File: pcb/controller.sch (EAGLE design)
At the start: 5 parts, among them IC1 74LS595D, IC2 74LS595D, IC3 FT232RL, U1 ATMEGA328P-PU, X1 MINI-USB_SHIELD5P4-32005-400

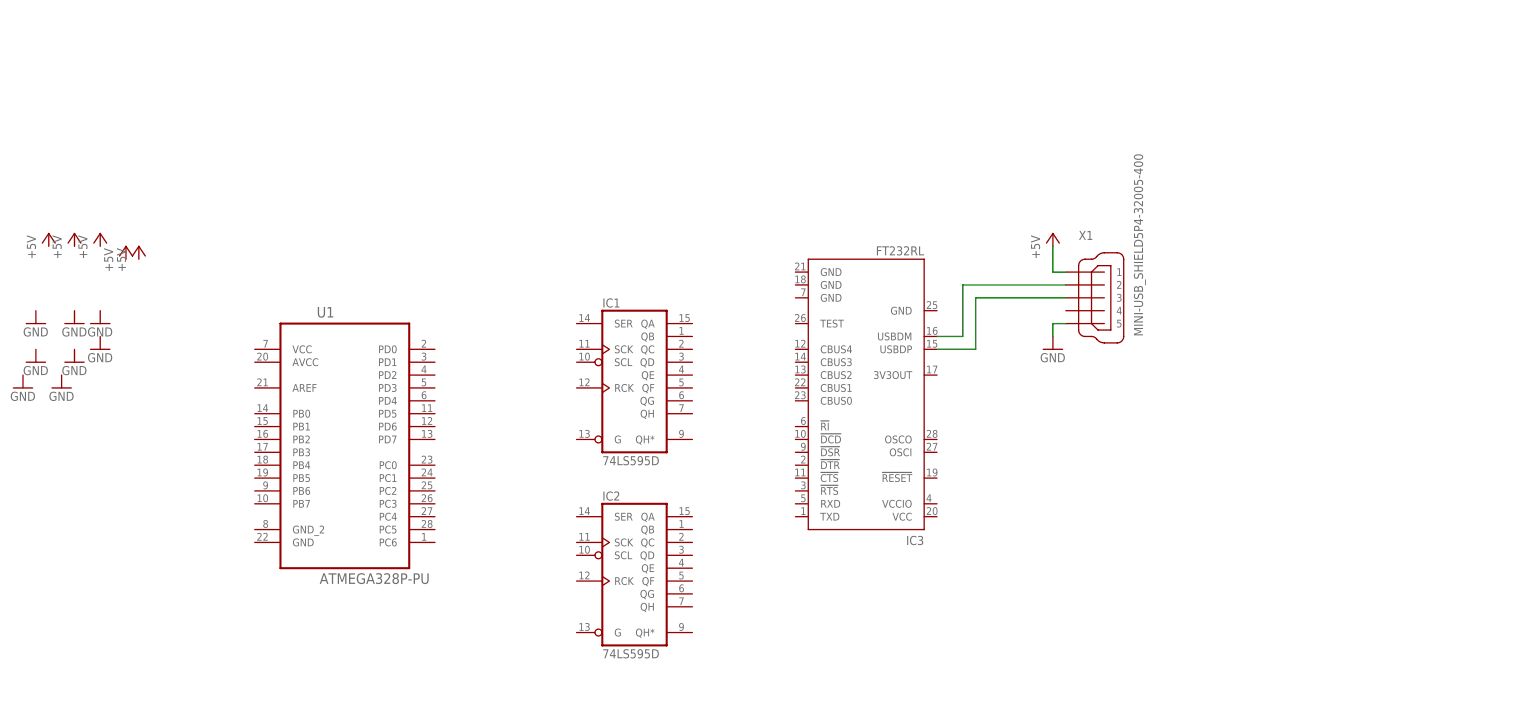
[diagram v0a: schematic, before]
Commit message: Connected FTDI and atmega328
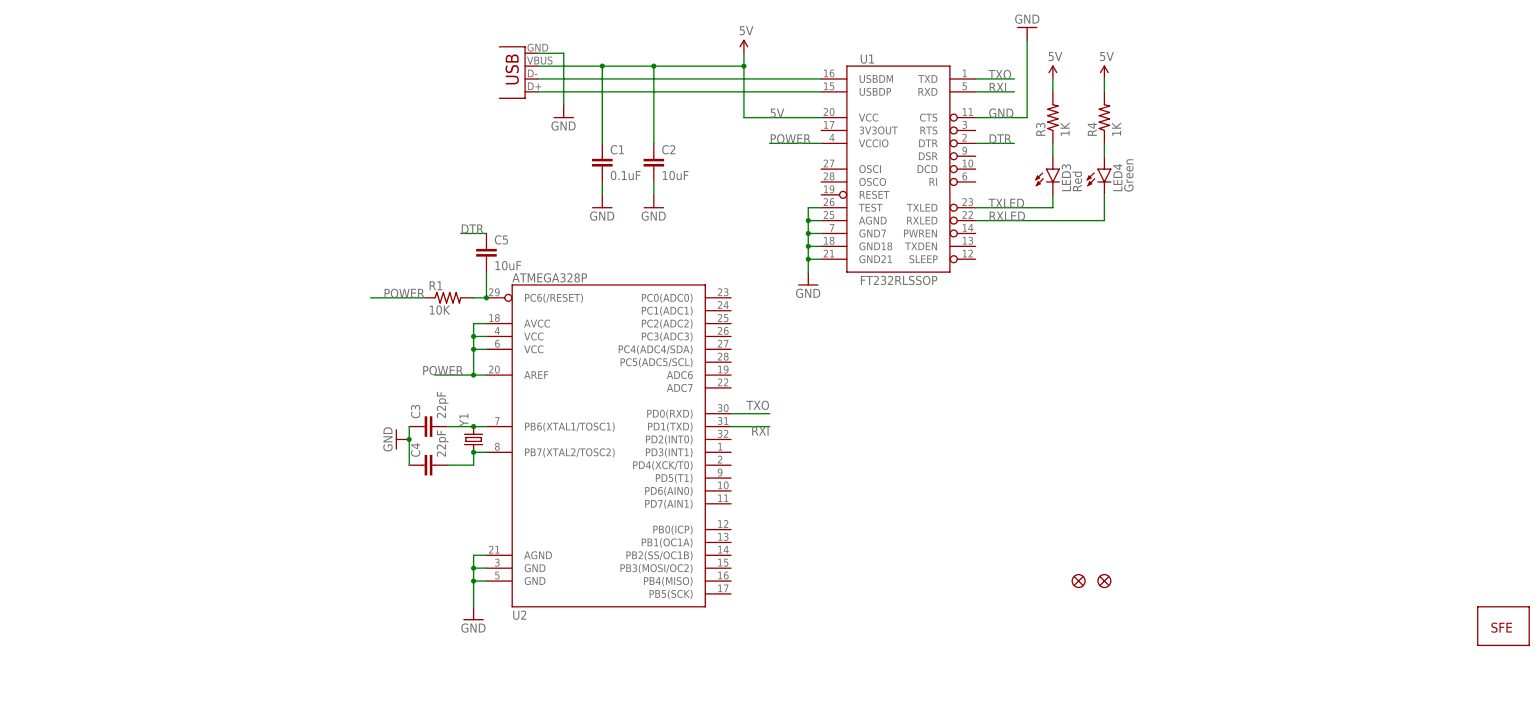
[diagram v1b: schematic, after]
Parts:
- removed IC1, IC2: 74LS595D, 74xx-us:74LS595D
- removed IC3: FT232RL, ftdichip:FT232RL
- removed X1: MINI-USB_SHIELD5P4-32005-400, con-cypressindustries:MINI-USB_SHIELD5P4-32005-400
- added C1: 0.1uF, SparkFun-Capacitors:CAP0805
- added C2, C5: 10uF, SparkFun-Capacitors:CAP0805
- added C3, C4: 22pF, SparkFun-Capacitors:CAP0805
- added JP8, JP9: FIDUCIAL1X2, SparkFun:FIDUCIAL1X2
- added LED3: Red, SparkFun-LED:LED1206
- added LED4: Green, SparkFun-LED:LED1206
- added R1: 10K, SparkFun-Resistors:RESISTOR0805-RES
- added R3, R4: 1K, SparkFun-Resistors:RESISTOR0805-RES
- added U$2: LOGO-SFENW2, SparkFun:LOGO-SFENW2
- added U2: ATMEGA328P, SparkFun-DigitalIC:ATMEGA328_SMT
- added X2: USB-SMD-NS, SparkFun:USB-SMD-NS
- added Y1: (no value), SparkFun-FreqCtrl:CRYSTALHC49US
- U1: value ATMEGA328P-PU -> FT232RLSSOP; device Atmel_By_element14_Batch_1-00:ATMEGA328P-PU -> SparkFun:FT232RLSSOP
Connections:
- removed net +5V: X1G$1.1
- new net 5V: C1.1, C2.1, R3.2, R4.2, U1.VCC, X2.VBUS
- new net DTR: C5.1, U1.DTR
- new net N$3: C5.2, R1.2, U2.PC6(/RESET)
- new net N$7: C3.2, U2.PB6(XTAL1/TOSC1), Y1.2
- new net N$8: C4.2, U2.PB7(XTAL2/TOSC2), Y1.1
- new net POWER: R1.1, U1.VCCIO, U2.AREF, U2.AVCC, U2.VCC@1, U2.VCC@2
- new net RXI: U1.RXD, U2.PD1(TXD)
- new net RXLED: LED4.C, U1.RXLED
- new net TXLED: LED3.C, U1.TXLED
- new net TXO: U1.TXD, U2.PD0(RXD)
- new net USB_D+: U1.USBDP, X2.D+
- new net USB_D-: U1.USBDM, X2.D-
- net GND: now also C1.2, C2.2, C3.1, C4.1, U1.AGND, U1.CTS, U1.GND18, U1.GND21, U1.GND7, U1.TEST, U2.AGND, U2.GND@1, U2.GND@2, X2.GND; no longer X1G$1.5
- net N$1: now also LED3.A, R3.1; no longer IC3.USBDM, X1G$1.2
- net N$2: now also LED4.A, R4.1; no longer IC3.USBDP, X1G$1.3

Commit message: Added ISCP to atmega328
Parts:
- added ICSP: (no value), SparkFun-Connectors:M03X2POGO_PINS
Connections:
- removed net N$3: C5.2, R1.2, U2.PC6(/RESET)
- new net MISO: ICSP.1, U2.PB4(MISO)
- new net MOSI: ICSP.4, U2.PB3(MOSI/OC2)
- new net RESET: C5.2, ICSP.5, R1.2, U2.PC6(/RESET)
- new net SCK: ICSP.3, U2.PB5(SCK)
- net GND: now also ICSP.6
- net POWER: now also ICSP.2
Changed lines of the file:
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@@
 <part name="C5" library="SparkFun-Capacitors" deviceset="CAP" device="0805" value="10uF"/>
 <part name="GND4" library="SparkFun" deviceset="GND" device=""/>
+<part name="ICSP" library="SparkFun-Connectors" deviceset="M03X2" device="POGO_PINS"/>
 </parts>
 <sheets>
@@
 <instance part="C5" gate="G$1" x="43.18" y="91.44"/>
 <instance part="GND4" gate="1" x="149.86" y="137.16" rot="R180"/>
+<instance part="ICSP" gate="G$1" x="68.58" y="10.16"/>
 </instances>
 <busses>
@@
 <pinref part="GND4" gate="1" pin="GND"/>
 </segment>
+<segment>
+<pinref part="ICSP" gate="G$1" pin="6"/>
+<wire x1="76.2" y1="7.62" x2="83.82" y2="7.62" width="0.1524" layer="91"/>
+<label x="76.2" y="7.62" size="1.778" layer="95"/>
+</segment>
 </net>
 <net name="USB_D-" class="0">
@@
 <wire x1="30.48" y1="83.82" x2="20.32" y2="83.82" width="0.1524" layer="91"/>
 <label x="22.86" y="83.82" size="1.778" layer="95"/>
+</segment>
+<segment>
+<pinref part="ICSP" gate="G$1" pin="2"/>
+<wire x1="76.2" y1="12.7" x2="83.82" y2="12.7" width="0.1524" layer="91"/>
+<label x="76.2" y="12.7" size="1.778" layer="95"/>
 </segment>
 </net>
@@
 </segment>
 </net>
-<net name="N$3" class="0">
-<segment>
-<pinref part="U2" gate="G$1" pin="PC6(/RESET)"/>
-<wire x1="43.18" y1="83.82" x2="40.64" y2="83.82" width="0.1524" layer="91"/>
-<pinref part="R1" gate="G$1" pin="2"/>
-<pinref part="C5" gate="G$1" pin="2"/>
-<wire x1="43.18" y1="83.82" x2="43.18" y2="88.9" width="0.1524" layer="91"/>
-<junction x="43.18" y="83.82"/>
-</segment>
-</net>
 <net name="N$7" class="0">
 <segment>
@@
 </segment>
 </net>
+<net name="MISO" class="0">
+<segment>
+<pinref part="ICSP" gate="G$1" pin="1"/>
+<wire x1="60.96" y1="12.7" x2="53.34" y2="12.7" width="0.1524" layer="91"/>
+<label x="53.34" y="12.7" size="1.778" layer="95"/>
+</segment>
+<segment>
+<pinref part="U2" gate="G$1" pin="PB4(MISO)"/>
+<wire x1="91.44" y1="27.94" x2="99.06" y2="27.94" width="0.1524" layer="91"/>
+<label x="93.98" y="27.94" size="1.778" layer="95"/>
+</segment>
+</net>
+<net name="SCK" class="0">
+<segment>
+<pinref part="ICSP" gate="G$1" pin="3"/>
+<wire x1="60.96" y1="10.16" x2="53.34" y2="10.16" width="0.1524" layer="91"/>
+<label x="53.34" y="10.16" size="1.778" layer="95"/>
+</segment>
+<segment>
+<pinref part="U2" gate="G$1" pin="PB5(SCK)"/>
+<wire x1="91.44" y1="25.4" x2="99.06" y2="25.4" width="0.1524" layer="91"/>
+<label x="93.98" y="25.4" size="1.778" layer="95"/>
+</segment>
+</net>
+<net name="RESET" class="0">
+<segment>
+<pinref part="ICSP" gate="G$1" pin="5"/>
+<wire x1="60.96" y1="7.62" x2="53.34" y2="7.62" width="0.1524" layer="91"/>
+<label x="53.34" y="7.62" size="1.778" layer="95"/>
+</segment>
+<segment>
+<pinref part="U2" gate="G$1" pin="PC6(/RESET)"/>
+<wire x1="43.18" y1="83.82" x2="40.64" y2="83.82" width="0.1524" layer="91"/>
+<pinref part="R1" gate="G$1" pin="2"/>
+<pinref part="C5" gate="G$1" pin="2"/>
+<wire x1="43.18" y1="83.82" x2="43.18" y2="88.9" width="0.1524" layer="91"/>
+<junction x="43.18" y="83.82"/>
+<wire x1="43.18" y1="83.82" x2="35.56" y2="91.44" width="0.1524" layer="91"/>
+<wire x1="35.56" y1="91.44" x2="27.94" y2="91.44" width="0.1524" layer="91"/>
+<label x="27.94" y="91.44" size="1.778" layer="95"/>
+</segment>
+</net>
+<net name="MOSI" class="0">
+<segment>
+<pinref part="ICSP" gate="G$1" pin="4"/>
+<wire x1="76.2" y1="10.16" x2="83.82" y2="10.16" width="0.1524" layer="91"/>
+<label x="76.2" y="10.16" size="1.778" layer="95"/>
+</segment>
+<segment>
+<pinref part="U2" gate="G$1" pin="PB3(MOSI/OC2)"/>
+<wire x1="91.44" y1="30.48" x2="99.06" y2="30.48" width="0.1524" layer="91"/>
+<label x="93.98" y="30.48" size="1.778" layer="95"/>
+</segment>
+</net>

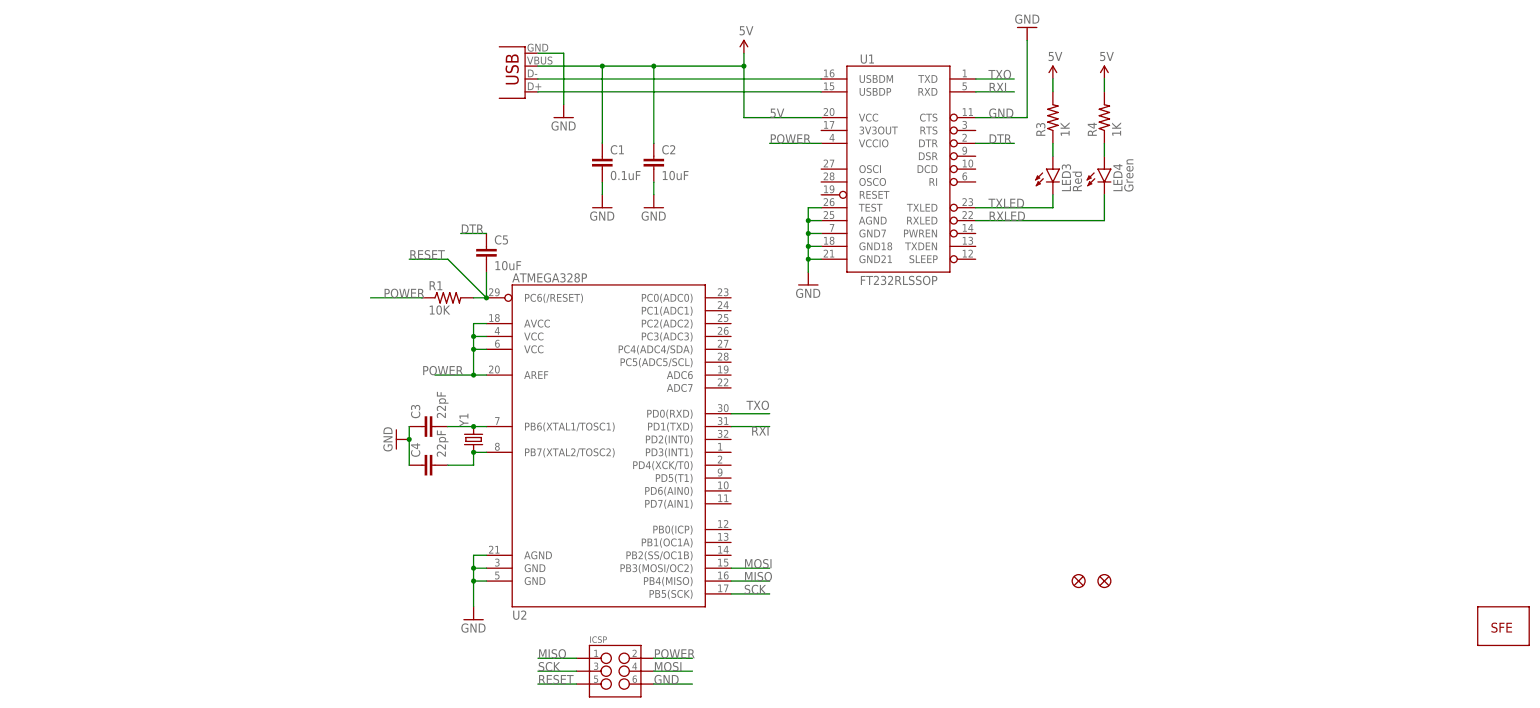
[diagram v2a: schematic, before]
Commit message: Connected 2 74hc595 to the atmega328
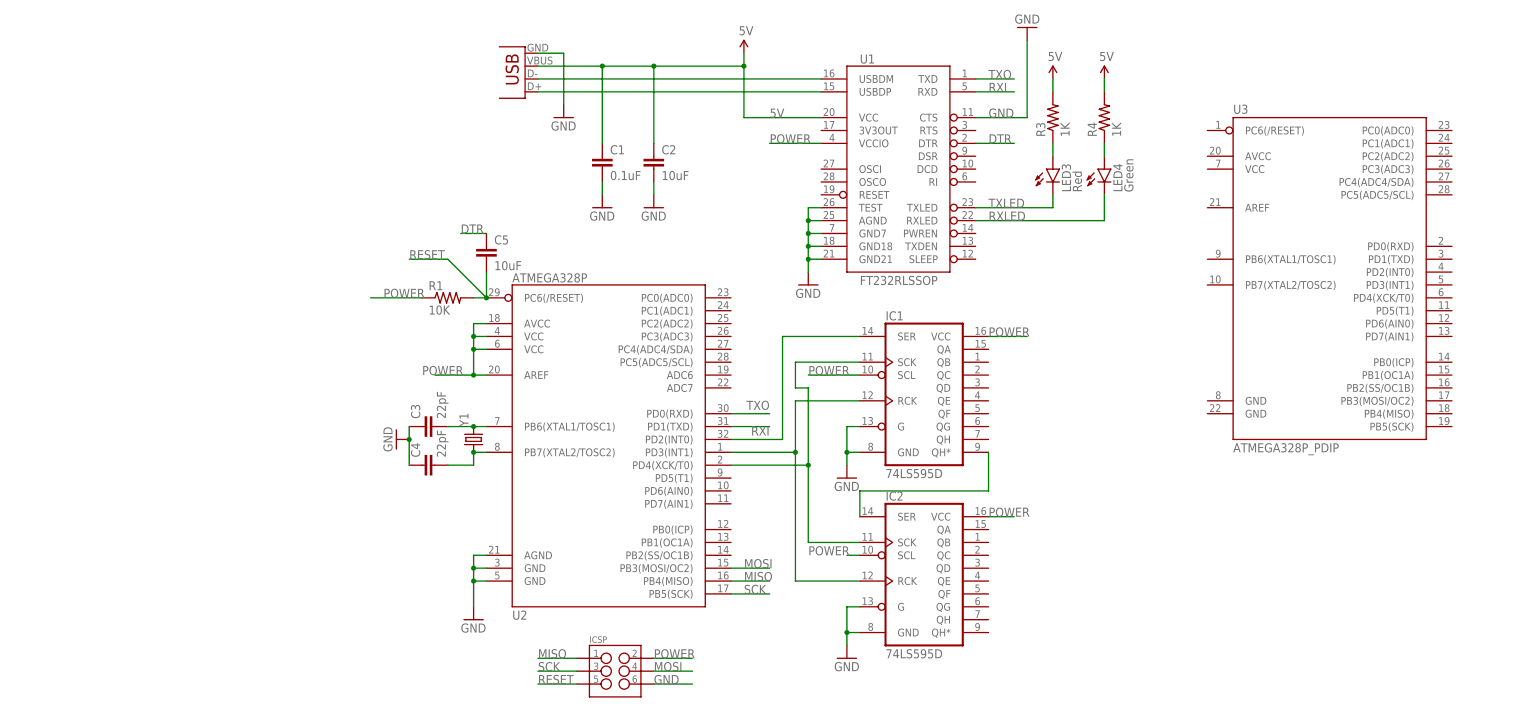
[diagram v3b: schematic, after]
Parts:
- removed JP8, JP9: FIDUCIAL1X2, SparkFun:FIDUCIAL1X2
- removed U$2: LOGO-SFENW2, SparkFun:LOGO-SFENW2
- added IC1, IC2: 74LS595D, SparkFun-DigitalIC:74LS595D
- added U3: ATMEGA328P_PDIP, SparkFun-DigitalIC:ATMEGA328P_PDIP
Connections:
- new net N$3: IC1.QH*, IC2.SER
- new net N$4: IC1.SER, U2.PD2(INT0)
- new net N$5: IC1.RCK, IC2.RCK, U2.PD3(INT1)
- new net N$6: IC1.SCK, IC2.SCK, U2.PD4(XCK/T0)
- net GND: now also IC1.G, IC1.GND, IC2.G, IC2.GND
- net POWER: now also IC1.SCL, IC1.VCC, IC2.SCL, IC2.VCC
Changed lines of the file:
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@@
 <part name="GND5" library="SparkFun" deviceset="GND" device=""/>
 <part name="FRAME1" library="SparkFun" deviceset="FRAME-LETTER" device=""/>
-<part name="U$2" library="SparkFun" deviceset="LOGO-SFE" device="NW2"/>
 <part name="U1" library="SparkFun" deviceset="FT232RL" device="SSOP"/>
 <part name="GND7" library="SparkFun" deviceset="GND" device=""/>
@@
 <part name="U$3" library="SparkFun" deviceset="5V" device=""/>
 <part name="U$4" library="SparkFun" deviceset="5V" device=""/>
-<part name="JP8" library="SparkFun" deviceset="FIDUCIAL" device="1X2"/>
-<part name="JP9" library="SparkFun" deviceset="FIDUCIAL" device="1X2"/>
 <part name="C1" library="SparkFun-Capacitors" deviceset="CAP" device="0805" value="0.1uF"/>
 <part name="C2" library="SparkFun-Capacitors" deviceset="CAP" device="0805" value="10uF"/>
@@
 <part name="GND4" library="SparkFun" deviceset="GND" device=""/>
 <part name="ICSP" library="SparkFun-Connectors" deviceset="M03X2" device="POGO_PINS"/>
+<part name="IC1" library="SparkFun-DigitalIC" deviceset="74*595" device="D" technology="LS"/>
+<part name="IC2" library="SparkFun-DigitalIC" deviceset="74*595" device="D" technology="LS"/>
+<part name="GND6" library="SparkFun" deviceset="GND" device=""/>
+<part name="GND9" library="SparkFun" deviceset="GND" device=""/>
+<part name="U3" library="SparkFun-DigitalIC" deviceset="ATMEGA328P_PDIP" device=""/>
 </parts>
 <sheets>
@@
 <instance part="FRAME1" gate="G$1" x="0" y="0"/>
 <instance part="FRAME1" gate="G$2" x="147.32" y="0"/>
-<instance part="U$2" gate="G$1" x="241.3" y="17.78"/>
 <instance part="U1" gate="G$1" x="124.46" y="109.22"/>
 <instance part="GND7" gate="1" x="66.04" y="101.6"/>
@@
 <instance part="U$3" gate="G$1" x="93.98" y="132.08"/>
 <instance part="U$4" gate="G$1" x="165.1" y="127"/>
-<instance part="JP8" gate="G$1" x="160.02" y="27.94"/>
-<instance part="JP9" gate="G$1" x="165.1" y="27.94"/>
 <instance part="C1" gate="G$1" x="66.04" y="109.22"/>
 <instance part="C2" gate="G$1" x="76.2" y="109.22"/>
@@
 <instance part="GND4" gate="1" x="149.86" y="137.16" rot="R180"/>
 <instance part="ICSP" gate="G$1" x="68.58" y="10.16"/>
+<instance part="IC1" gate="A" x="127" y="66.04"/>
+<instance part="IC2" gate="A" x="127" y="30.48"/>
+<instance part="GND6" gate="1" x="114.3" y="12.7"/>
+<instance part="GND9" gate="1" x="114.3" y="48.26"/>
+<instance part="U3" gate="G$1" x="208.28" y="91.44"/>
 </instances>
 <busses>
@@
 <label x="76.2" y="7.62" size="1.778" layer="95"/>
 </segment>
+<segment>
+<pinref part="IC2" gate="A" pin="G"/>
+<wire x1="116.84" y1="22.86" x2="114.3" y2="22.86" width="0.1524" layer="91"/>
+<wire x1="114.3" y1="22.86" x2="114.3" y2="17.78" width="0.1524" layer="91"/>
+<pinref part="IC2" gate="A" pin="GND"/>
+<wire x1="114.3" y1="17.78" x2="114.3" y2="15.24" width="0.1524" layer="91"/>
+<wire x1="116.84" y1="17.78" x2="114.3" y2="17.78" width="0.1524" layer="91"/>
+<junction x="114.3" y="17.78"/>
+<pinref part="GND6" gate="1" pin="GND"/>
+</segment>
+<segment>
+<pinref part="IC1" gate="A" pin="G"/>
+<wire x1="116.84" y1="58.42" x2="114.3" y2="58.42" width="0.1524" layer="91"/>
+<wire x1="114.3" y1="58.42" x2="114.3" y2="53.34" width="0.1524" layer="91"/>
+<pinref part="IC1" gate="A" pin="GND"/>
+<wire x1="114.3" y1="53.34" x2="114.3" y2="50.8" width="0.1524" layer="91"/>
+<wire x1="116.84" y1="53.34" x2="114.3" y2="53.34" width="0.1524" layer="91"/>
+<junction x="114.3" y="53.34"/>
+<pinref part="GND9" gate="1" pin="GND"/>
+</segment>
 </net>
 <net name="USB_D-" class="0">
@@
 <wire x1="76.2" y1="12.7" x2="83.82" y2="12.7" width="0.1524" layer="91"/>
 <label x="76.2" y="12.7" size="1.778" layer="95"/>
+</segment>
+<segment>
+<pinref part="IC1" gate="A" pin="SCL"/>
+<wire x1="116.84" y1="68.58" x2="106.68" y2="68.58" width="0.1524" layer="91"/>
+<label x="106.68" y="68.58" size="1.778" layer="95"/>
+</segment>
+<segment>
+<pinref part="IC1" gate="A" pin="VCC"/>
+<wire x1="142.24" y1="76.2" x2="149.86" y2="76.2" width="0.1524" layer="91"/>
+<label x="142.24" y="76.2" size="1.778" layer="95"/>
+</segment>
+<segment>
+<pinref part="IC2" gate="A" pin="VCC"/>
+<wire x1="142.24" y1="40.64" x2="147.32" y2="40.64" width="0.1524" layer="91"/>
+<label x="142.24" y="40.64" size="1.778" layer="95"/>
+</segment>
+<segment>
+<pinref part="IC2" gate="A" pin="SCL"/>
+<wire x1="116.84" y1="33.02" x2="114.3" y2="33.02" width="0.1524" layer="91"/>
+<label x="106.68" y="33.02" size="1.778" layer="95"/>
 </segment>
 </net>
@@
 </segment>
 </net>
+<net name="N$3" class="0">
+<segment>
+<pinref part="IC1" gate="A" pin="QH*"/>
+<wire x1="142.24" y1="53.34" x2="142.24" y2="45.72" width="0.1524" layer="91"/>
+<wire x1="142.24" y1="45.72" x2="116.84" y2="45.72" width="0.1524" layer="91"/>
+<pinref part="IC2" gate="A" pin="SER"/>
+<wire x1="116.84" y1="45.72" x2="116.84" y2="40.64" width="0.1524" layer="91"/>
+</segment>
+</net>
+<net name="N$4" class="0">
+<segment>
+<pinref part="U2" gate="G$1" pin="PD2(INT0)"/>
+<wire x1="91.44" y1="55.88" x2="101.6" y2="55.88" width="0.1524" layer="91"/>
+<wire x1="101.6" y1="55.88" x2="101.6" y2="76.2" width="0.1524" layer="91"/>
+<pinref part="IC1" gate="A" pin="SER"/>
+<wire x1="101.6" y1="76.2" x2="116.84" y2="76.2" width="0.1524" layer="91"/>
+</segment>
+</net>
+<net name="N$5" class="0">
+<segment>
+<pinref part="U2" gate="G$1" pin="PD3(INT1)"/>
+<wire x1="91.44" y1="53.34" x2="104.14" y2="53.34" width="0.1524" layer="91"/>
+<wire x1="104.14" y1="53.34" x2="104.14" y2="63.5" width="0.1524" layer="91"/>
+<pinref part="IC1" gate="A" pin="RCK"/>
+<wire x1="104.14" y1="63.5" x2="116.84" y2="63.5" width="0.1524" layer="91"/>
+<wire x1="104.14" y1="53.34" x2="104.14" y2="27.94" width="0.1524" layer="91"/>
+<pinref part="IC2" gate="A" pin="RCK"/>
+<wire x1="104.14" y1="27.94" x2="116.84" y2="27.94" width="0.1524" layer="91"/>
+<junction x="104.14" y="53.34"/>
+</segment>
+</net>
+<net name="N$6" class="0">
+<segment>
+<pinref part="U2" gate="G$1" pin="PD4(XCK/T0)"/>
+<wire x1="91.44" y1="50.8" x2="106.68" y2="50.8" width="0.1524" layer="91"/>
+<wire x1="106.68" y1="50.8" x2="106.68" y2="35.56" width="0.1524" layer="91"/>
+<pinref part="IC2" gate="A" pin="SCK"/>
+<wire x1="106.68" y1="35.56" x2="116.84" y2="35.56" width="0.1524" layer="91"/>
+<wire x1="106.68" y1="50.8" x2="106.68" y2="66.04" width="0.1524" layer="91"/>
+<pinref part="IC1" gate="A" pin="SCK"/>
+<wire x1="104.14" y1="71.12" x2="116.84" y2="71.12" width="0.1524" layer="91"/>
+<wire x1="104.14" y1="66.04" x2="104.14" y2="71.12" width="0.1524" layer="91"/>
+<wire x1="106.68" y1="66.04" x2="104.14" y2="66.04" width="0.1524" layer="91"/>
+<junction x="106.68" y="50.8"/>
+</segment>
+</net>
